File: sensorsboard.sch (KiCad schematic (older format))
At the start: 45 parts, among them J1 Conn_01x05_Female, J2 USB_B_Micro, J3 Conn_01x03_Female, J4 SWD, J5 Conn_01x02_Male, J6 Conn_01x03_Male, J7 USB_B_Micro, J8 Conn_02x05_Odd_Even, J9 UART, SW1 nRF_Reset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

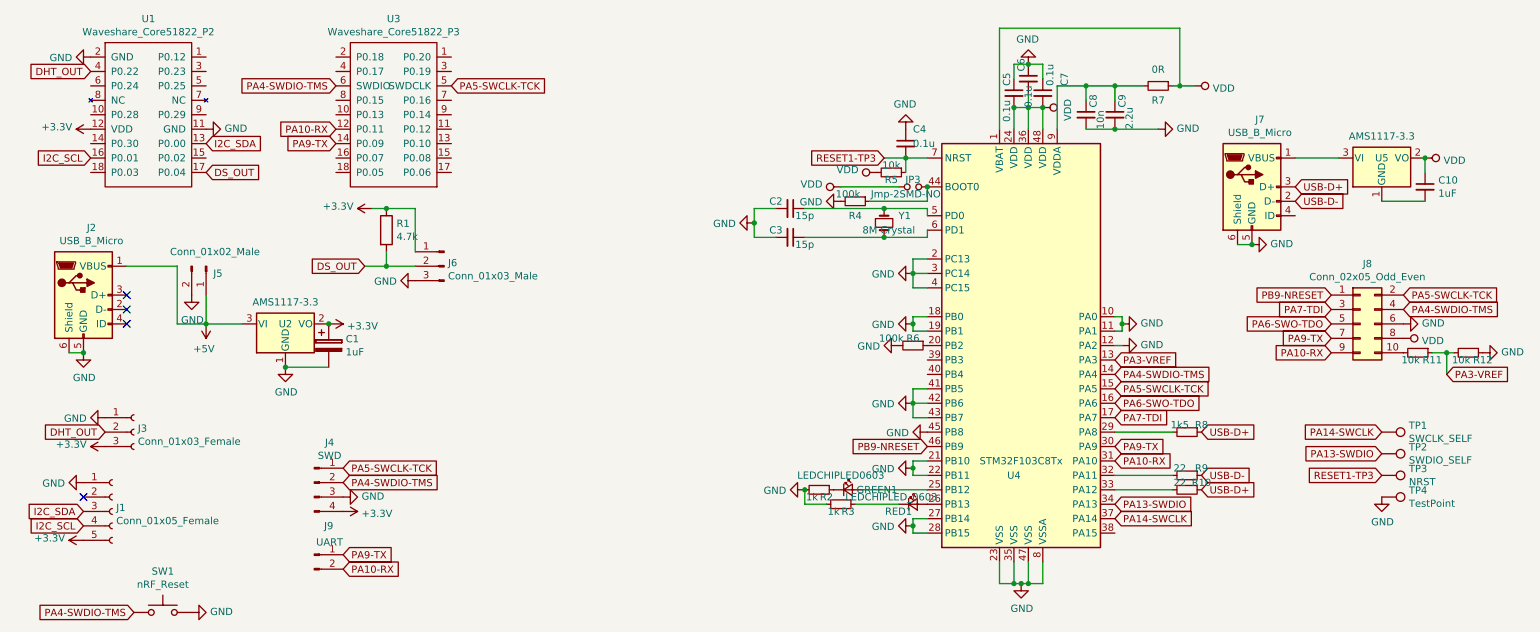
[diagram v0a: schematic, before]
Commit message: Fix AMS1117 GND connection
Signed-off-by: Zamir SUN <sztsian@gmail.com>
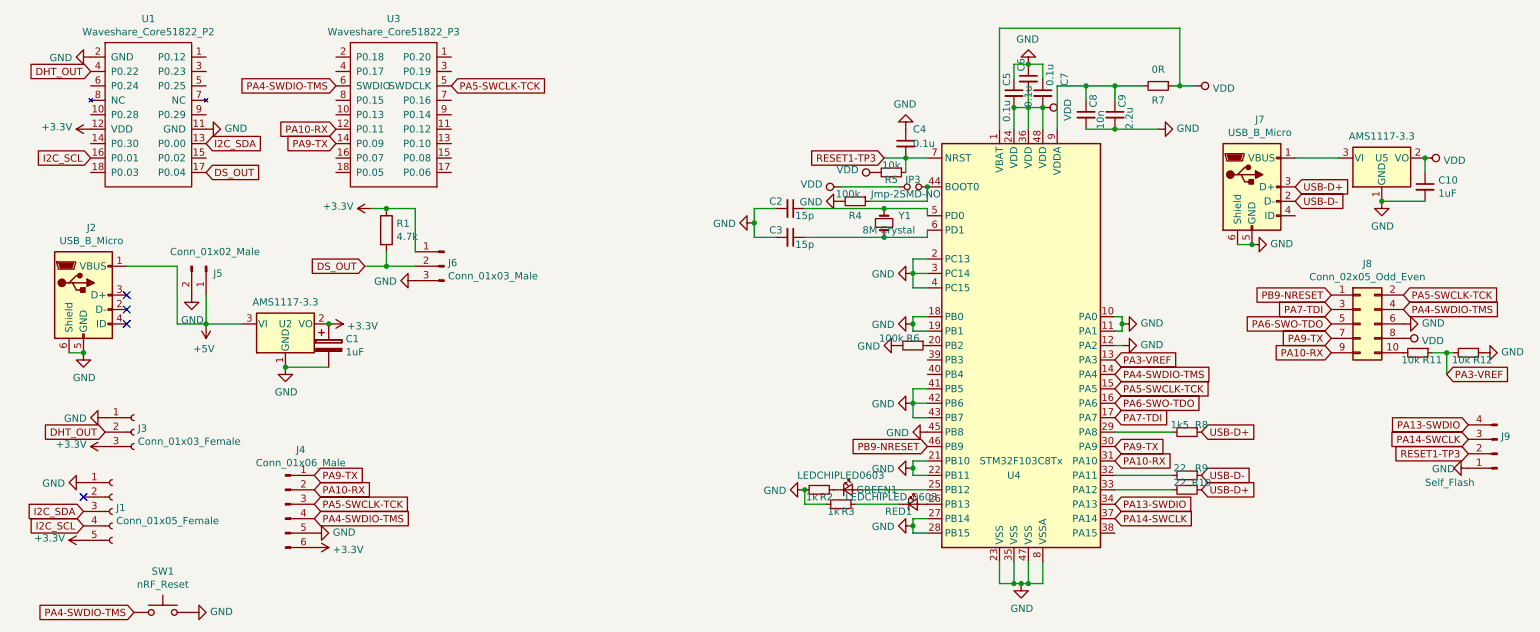
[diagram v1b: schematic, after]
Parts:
- removed J4: SWD, Connector_PinHeader_2.54mm:PinHeader_1x04_P2.54mm_Vertical, symbol Connector:Conn_01x04_Male
- removed J9: UART, Connector_PinHeader_2.54mm:PinHeader_1x02_P2.54mm_Vertical, symbol Connector:Conn_01x02_Male
- removed TP1: SWCLK_SELF, TestPoint:TestPoint_THTPad_D2.0mm_Drill1.0mm, symbol Connector:TestPoint
- removed TP2: SWDIO_SELF, TestPoint:TestPoint_THTPad_D2.0mm_Drill1.0mm, symbol Connector:TestPoint
- removed TP3: NRST, TestPoint:TestPoint_THTPad_D2.0mm_Drill1.0mm, symbol Connector:TestPoint
- removed TP4: TestPoint, TestPoint:TestPoint_THTPad_D2.0mm_Drill1.0mm, symbol Connector:TestPoint
- added J4: Conn_01x06_Male, Connector_PinHeader_2.54mm:PinHeader_1x06_P2.54mm_Vertical, symbol Connector:Conn_01x06_Male
- added J9: Self_Flash, Connector_PinHeader_2.54mm:PinHeader_1x04_P2.54mm_Vertical, symbol Connector:Conn_01x04_Male
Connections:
- net +3V3: now also J4.6 (Pin_6)
- net GND: now also C10.2, U5.1 (GND), J4.5 (Pin_5), J9.1 (Pin_1)
- net PA10-RX: now also J4.2 (Pin_2)
- net PA13-SWDIO: now also J9.4 (Pin_4)
- net PA14-SWCLK: now also J9.3 (Pin_3)
- net PA4-SWDIO-TMS: now also J4.4 (Pin_4)
- net PA5-SWCLK-TCK: now also J4.3 (Pin_3)
- net PA9-TX: now also J4.1 (Pin_1)
- net RESET1-TP3: now also J9.2 (Pin_2)
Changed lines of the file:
@@
-	1    0    0    -1
-$EndComp
-$Comp
-L Connector:Conn_01x04_Male J4
-U 1 1 5C796D41
-P 2750 4000
-F 0 "J4" H 2856 4278 50  0000 C CNN
-F 1 "SWD" H 2856 4187 50  0000 C CNN
-F 2 "Connector_PinHeader_2.54mm:PinHeader_1x04_P2.54mm_Vertical" H 2750 4000 50  0001 C CNN
-F 3 "~" H 2750 4000 50  0001 C CNN
-	1    2750 4000
 	1    0    0    -1
 $EndComp
@@
 L power:GND #PWR08
 U 1 1 5C7983EC
-P 2950 4100
-F 0 "#PWR08" H 2950 3850 50  0001 C CNN
-F 1 "GND" V 2955 3972 50  0000 R CNN
-F 2 "" H 2950 4100 50  0001 C CNN
-F 3 "" H 2950 4100 50  0001 C CNN
-	1    2950 4100
+P 2750 4350
+F 0 "#PWR08" H 2750 4100 50  0001 C CNN
+F 1 "GND" V 2755 4222 50  0000 R CNN
+F 2 "" H 2750 4350 50  0001 C CNN
+F 3 "" H 2750 4350 50  0001 C CNN
+	1    2750 4350
 	0    -1   -1   0
 $EndComp
@@
 L power:+3.3V #PWR09
 U 1 1 5C798971
-P 2950 4200
-F 0 "#PWR09" H 2950 4050 50  0001 C CNN
-F 1 "+3.3V" V 2965 4328 50  0000 L CNN
-F 2 "" H 2950 4200 50  0001 C CNN
-F 3 "" H 2950 4200 50  0001 C CNN
-	1    2950 4200
+P 2750 4450
+F 0 "#PWR09" H 2750 4300 50  0001 C CNN
+F 1 "+3.3V" V 2765 4578 50  0000 L CNN
+F 2 "" H 2750 4450 50  0001 C CNN
+F 3 "" H 2750 4450 50  0001 C CNN
+	1    2750 4450
 	0    1    1    0
 $EndComp
@@
 Wire Wire Line
 	10600 3100 10650 3100
-$Comp
-L Connector:TestPoint TP1
-U 1 1 5C7DD15B
-P 10150 3650
-F 0 "TP1" V 10104 3837 50  0000 L CNN
-F 1 "SWCLK_SELF" V 10195 3837 50  0000 L CNN
-F 2 "TestPoint:TestPoint_THTPad_D2.0mm_Drill1.0mm" H 10350 3650 50  0001 C CNN
-F 3 "~" H 10350 3650 50  0001 C CNN
-	1    10150 3650
-	0    1    1    0
-$EndComp
-$Comp
-L Connector:TestPoint TP2
-U 1 1 5C7DFB91
-P 10150 3800
-F 0 "TP2" V 10104 3988 50  0000 L CNN
-F 1 "SWDIO_SELF" V 10195 3988 50  0000 L CNN
-F 2 "TestPoint:TestPoint_THTPad_D2.0mm_Drill1.0mm" H 10350 3800 50  0001 C CNN
-F 3 "~" H 10350 3800 50  0001 C CNN
-	1    10150 3800
-	0    1    1    0
-$EndComp
-$Comp
-L Connector:TestPoint TP3
-U 1 1 5C7DFC88
-P 10150 3950
-F 0 "TP3" V 10104 4138 50  0000 L CNN
-F 1 "NRST" V 10195 4138 50  0000 L CNN
-F 2 "TestPoint:TestPoint_THTPad_D2.0mm_Drill1.0mm" H 10350 3950 50  0001 C CNN
-F 3 "~" H 10350 3950 50  0001 C CNN
-	1    10150 3950
-	0    1    1    0
-$EndComp
-$Comp
-L Connector:TestPoint TP4
-U 1 1 5C7E1747
-P 10150 4100
-F 0 "TP4" V 10104 4288 50  0000 L CNN
-F 1 "TestPoint" V 10195 4288 50  0000 L CNN
-F 2 "TestPoint:TestPoint_THTPad_D2.0mm_Drill1.0mm" H 10350 4100 50  0001 C CNN
-F 3 "~" H 10350 4100 50  0001 C CNN
-	1    10150 4100
-	0    1    1    0
-$EndComp
 Text GLabel 6700 1750 0    50   Input ~ 0
 RESET1-TP3
-Text GLabel 10150 3650 0    50   Input ~ 0
+Text GLabel 10750 3700 0    50   Input ~ 0
 PA14-SWCLK
-Text GLabel 10150 3800 0    50   Input ~ 0
+Text GLabel 10750 3600 0    50   Input ~ 0
 PA13-SWDIO
-Text GLabel 10150 3950 0    50   Input ~ 0
+Text GLabel 10750 3800 0    50   Input ~ 0
 RESET1-TP3
 $Comp
 L power:GND #PWR035
 U 1 1 5C7F068D
-P 10150 4100
-F 0 "#PWR035" H 10150 3850 50  0001 C CNN
-F 1 "GND" H 10155 3927 50  0000 C CNN
-F 2 "" H 10150 4100 50  0001 C CNN
-F 3 "" H 10150 4100 50  0001 C CNN
-	1    10150 4100
-	1    0    0    -1
+P 10750 3900
+F 0 "#PWR035" H 10750 3650 50  0001 C CNN
+F 1 "GND" V 10755 3727 50  0000 C CNN
+F 2 "" H 10750 3900 50  0001 C CNN
+F 3 "" H 10750 3900 50  0001 C CNN
+	1    10750 3900
+	0    1    1    0
 $EndComp
 Text GLabel 9800 3000 0    50   Input ~ 0
@@
 Text GLabel 2900 1550 0    50   Input ~ 0
 PA10-RX
-$Comp
-L Connector:Conn_01x02_Male J9
-U 1 1 5C7CB96E
-P 2750 4500
-F 0 "J9" H 2850 4700 50  0000 C CNN
-F 1 "UART" H 2856 4587 50  0000 C CNN
-F 2 "Connector_PinHeader_2.54mm:PinHeader_1x02_P2.54mm_Vertical" H 2750 4500 50  0001 C CNN
-F 3 "~" H 2750 4500 50  0001 C CNN
-	1    2750 4500
-	1    0    0    -1
-$EndComp
-Text GLabel 2950 4500 2    50   Input ~ 0
+Text GLabel 2750 3950 2    50   Input ~ 0
 PA9-TX
-Text GLabel 2950 4600 2    50   Input ~ 0
+Text GLabel 2750 4050 2    50   Input ~ 0
 PA10-RX
-Text GLabel 2950 4000 2    50   Input ~ 0
+Text GLabel 2750 4250 2    50   Input ~ 0
 PA4-SWDIO-TMS
-Text GLabel 2950 3900 2    50   Input ~ 0
+Text GLabel 2750 4150 2    50   Input ~ 0
 PA5-SWCLK-TCK
 Text GLabel 3700 1250 2    50   Input ~ 0
@@
 	2000 2900 2250 2900
 $Comp
-L power:+5V #PWR?
+L power:+5V #PWR040
 U 1 1 5C839423
 P 2000 2900
-F 0 "#PWR?" H 2000 2750 50  0001 C CNN
+F 0 "#PWR040" H 2000 2750 50  0001 C CNN
 F 1 "+5V" H 2015 3073 50  0000 C CNN
 F 2 "" H 2000 2900 50  0001 C CNN
@@
 Wire Wire Line
 	9550 1750 9850 1750
+$Comp
+L power:GND #PWR041
+U 1 1 5C8C9D72
+P 10150 2050
+F 0 "#PWR041" H 10150 1800 50  0001 C CNN
+F 1 "GND" H 10155 1877 50  0000 C CNN
+F 2 "" H 10150 2050 50  0001 C CNN
+F 3 "" H 10150 2050 50  0001 C CNN
+	1    10150 2050
+	1    0    0    -1
+$EndComp
+Connection ~ 10150 2050
+$Comp
+L Connector:Conn_01x06_Male J4
+U 1 1 5C8CE1DD
+P 2550 4150
+F 0 "J4" H 2656 4528 50  0000 C CNN
+F 1 "Conn_01x06_Male" H 2656 4437 50  0000 C CNN
+F 2 "Connector_PinHeader_2.54mm:PinHeader_1x06_P2.54mm_Vertical" H 2550 4150 50  0001 C CNN
+F 3 "~" H 2550 4150 50  0001 C CNN
+	1    2550 4150
+	1    0    0    -1
+$EndComp
+$Comp
+L Connector:Conn_01x04_Male J9
+U 1 1 5C8D5E24
+P 10950 3800
+F 0 "J9" H 10923 3680 50  0000 R CNN
+F 1 "Self_Flash" H 11450 4000 50  0000 R CNN
+F 2 "Connector_PinHeader_2.54mm:PinHeader_1x04_P2.54mm_Vertical" H 10950 3800 50  0001 C CNN
+F 3 "~" H 10950 3800 50  0001 C CNN
+	1    10950 3800
+	-1   0    0    1
+$EndComp
 $EndSCHEMATC

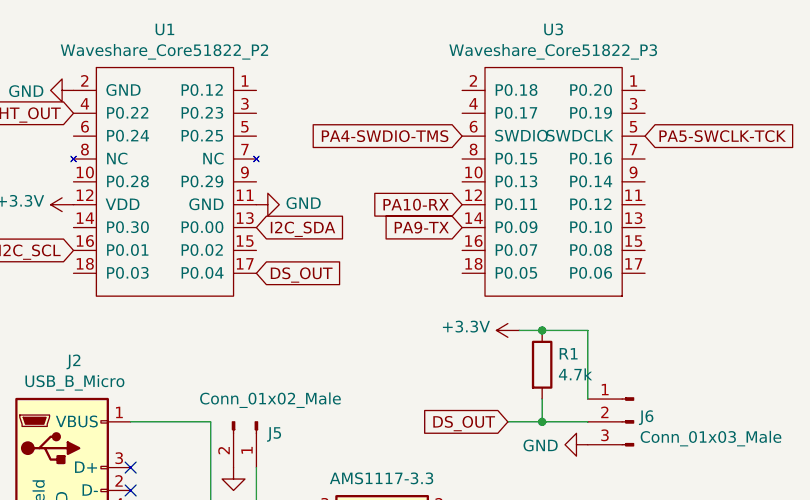
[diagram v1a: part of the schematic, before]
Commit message: Fix RX/TX connection to core51822
Signed-off-by: Zamir SUN <sztsian@gmail.com>
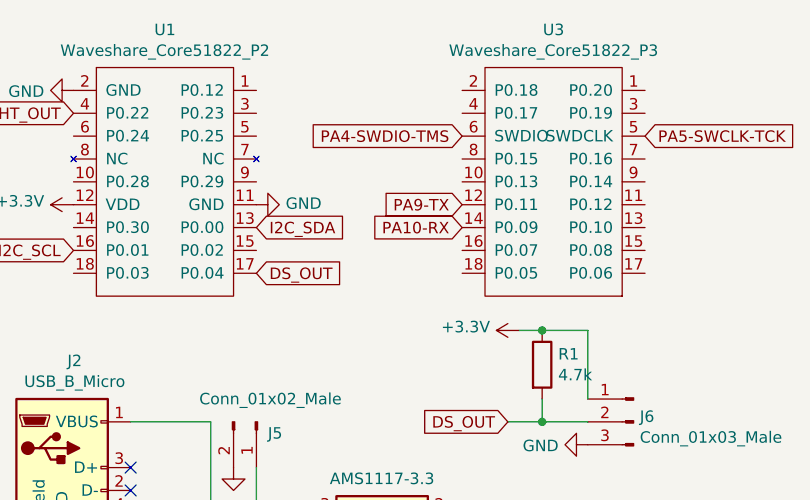
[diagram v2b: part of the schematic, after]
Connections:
- net PA10-RX: now also U3.14 (P0.09); no longer U3.12 (P0.11)
- net PA9-TX: now also U3.12 (P0.11); no longer U3.14 (P0.09)
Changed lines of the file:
@@
 $EndComp
 Connection ~ 9250 2350
+Text GLabel 2900 1550 0    50   Input ~ 0
+PA9-TX
 Text GLabel 2900 1650 0    50   Input ~ 0
-PA9-TX
-Text GLabel 2900 1550 0    50   Input ~ 0
 PA10-RX
 Text GLabel 2750 3950 2    50   Input ~ 0
